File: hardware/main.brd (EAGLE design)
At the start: 96.5 x 65.5 mm, 79 parts, among them U1 TMS320F28069_PN_80, U10 TXB0101_DBV_6, U2 TXB0101_DBV_6, U3 SN74ABT541B_DW_20, U4 SN74LVC1G04_DBV_5, U5 SN74LVC4245A_DW_24, U7 Value, U8 Value, U9 SN74LVC4245A_DW_24

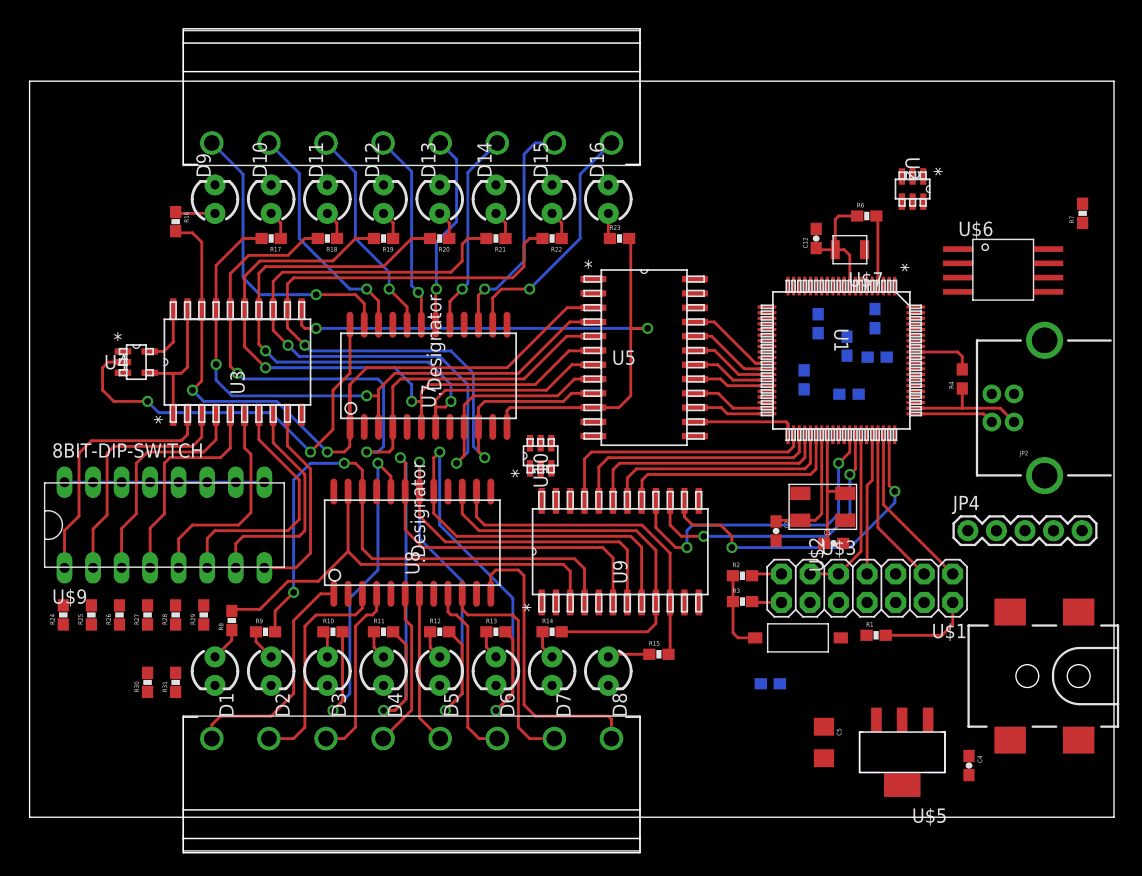
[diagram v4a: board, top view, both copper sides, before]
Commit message: Finished routing all signals traces. 3Vcc, 5Vcc, GND not yet routed. Signal traces need to be reviewed and cleaned up.
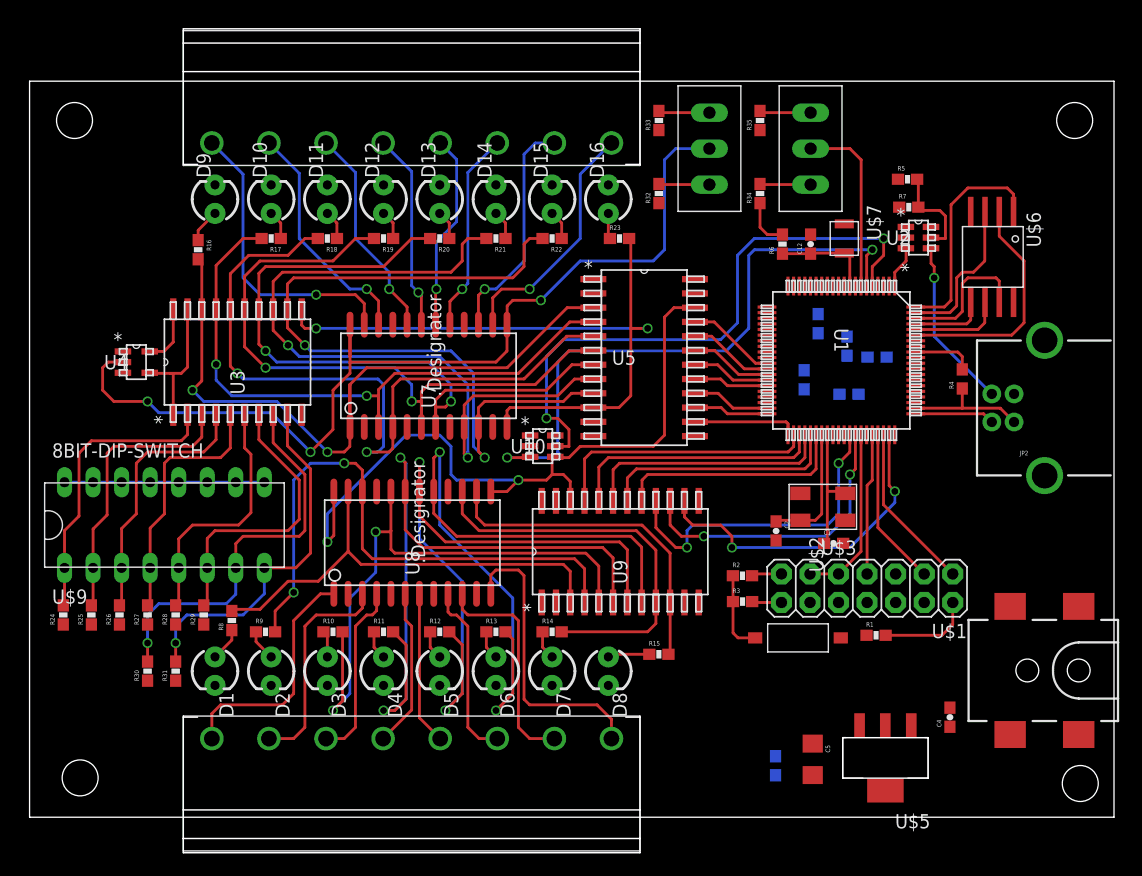
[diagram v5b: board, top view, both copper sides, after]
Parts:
- removed JP4: (no value), SparkFun-Connectors:1X05
- added R32, R33, R34, R35: 1K, SparkFun-Resistors:0603-RES
- added U$10, U$11: USER_SLIDE, ControllerCard:USER_SLIDE_SWITCH
- moved R7 15.5 mm to (78.2, 54.3), turned to 0 degrees
- moved R5 12.7 mm to (78.1, 56.8), flipped to the top, turned to 0 degrees
- moved R6 7.91 mm to (67.0, 51.0), turned to 90 degrees
- moved C6 7.31 mm to (66.4, 4.58), turned to 90 degrees
- moved C4 4.62 mm to (81.9, 8.90), turned to 90 degrees
- moved U2 4.35 mm to (79.1, 51.6), turned to 0 degrees
- moved R16 3.20 mm to (15.0, 50.5)
- moved C5 1.80 mm to (69.7, 5.15)
- moved U$5 1.58 mm to (76.2, 5.28)
- moved U$6 1.46 mm to (85.7, 49.9), turned to 270 degrees
- moved U$7 1.12 mm to (72.5, 51.5), turned to 270 degrees
- moved R30 1.00 mm to (10.5, 13.0)
- moved R31 1.00 mm to (13.0, 13.0)
- moved U10 0.88 mm to (45.7, 33.0), turned to 0 degrees
- moved C12 0.71 mm to (69.5, 51.0)
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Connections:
- new net N$29: R33.2, U$10.3
- new net N$38: R32.2, U$10.1
- new net N$39: R34.2, U$11.1
- new net N$40: R35.2, U$11.3
- net 3.3V: now also R34.1; no longer JP4.4
- net 5V: now also R32.1; no longer JP4.5
- net ENEXT: now also U1.5; no longer U1.7
- net GND: now also R33.1, R35.1; no longer JP4.1
- net INSEL: now also U$10.2; no longer JP4.3
- net RUNSEL: now also U$11.2, U1.7; no longer JP4.2, U1.5
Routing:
- net !BUFEN!: track 0.00 -> 65.9 mm, vias 0 -> 2
- net ENEXT: track 0.00 -> 61.7 mm, vias 0 -> 2
- net !ENEXT!: track 0.00 -> 55.2 mm, vias 0 -> 2
- net INSEL: track 37.6 -> 87.3 mm, vias 2 -> 3
- net SPISOMI: track 0.00 -> 20.9 mm
- net !FLASHEN!: track 0.00 -> 19.9 mm
- net LEDOUT3: track 34.0 -> 53.7 mm
- net RUNSEL: track 0.00 -> 16.2 mm
- net N$2: track 0.00 -> 15.2 mm, vias 0 -> 1
- net SW7: track 20.3 -> 35.4 mm, vias 0 -> 1
- net SW8: track 17.8 -> 32.4 mm, vias 0 -> 1
- net !FLASHWP!: track 0.00 -> 13.9 mm
- net !FLASHHOLD!: track 0.00 -> 12.4 mm
- net SPICLK: track 0.00 -> 8.26 mm
- net SPISIMO: track 0.00 -> 6.65 mm
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
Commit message: Finished re-routing clock and JTAG. Begun re-route of output stage.
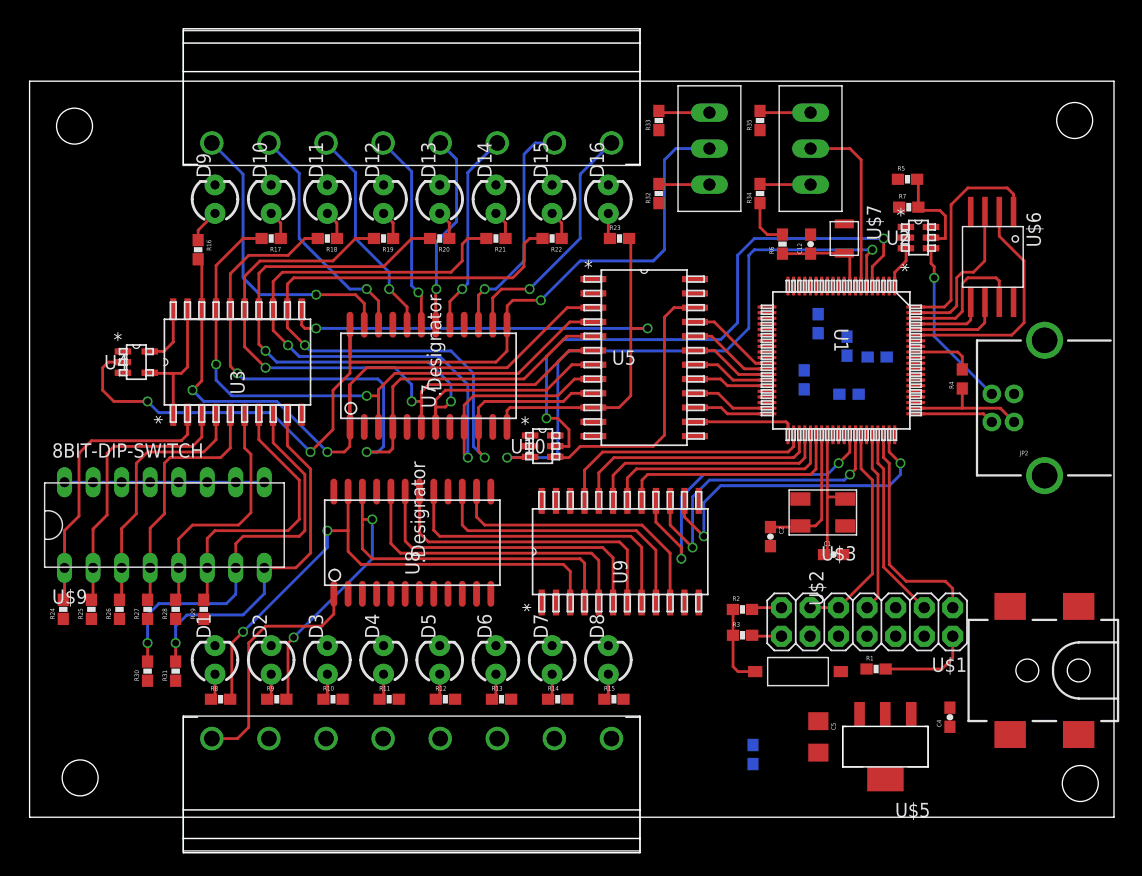
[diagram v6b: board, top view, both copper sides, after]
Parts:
- moved R8 7.07 mm to (17.0, 10.5), turned to 0 degrees
- moved R9 6.08 mm to (22.0, 10.5)
- moved R11 6.02 mm to (32.0, 10.5)
- moved R12 6.02 mm to (37.0, 10.5)
- moved R13 6.02 mm to (42.0, 10.5)
- moved R14 6.02 mm to (47.0, 10.5)
- moved R10 6.00 mm to (27.0, 10.5)
- moved R15 5.66 mm to (52.0, 10.5)
- moved R1 3.00 mm to (75.3, 13.2)
- moved R2 3.00 mm to (63.4, 18.5)
- moved R3 3.00 mm to (63.5, 16.2)
- moved U$1 3.00 mm to (82.2, 18.6)
- moved U$2 3.00 mm to (68.4, 13.0)
- moved C6 2.24 mm to (64.4, 5.58)
- moved C5 2.06 mm to (70.2, 7.15)
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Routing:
- net !BUFEN!: track 65.9 -> 24.3 mm, vias 2 -> 0
- net LEDOUT6: track 64.6 -> 27.5 mm, vias 2 -> 0
- net LEDOUT4: track 63.1 -> 27.5 mm, vias 2 -> 0
- net LEDOUT5: track 61.6 -> 27.5 mm, vias 2 -> 0
- net N$17: track 26.3 -> 0.00 mm
- net LEDOUT3: track 53.7 -> 27.5 mm, vias 2 -> 0
- net N$18: track 19.9 -> 0.00 mm
- net N$14: track 19.7 -> 0.00 mm
- net N$15: track 16.0 -> 0.00 mm
- net N$19: track 15.9 -> 0.00 mm
- net N$16: track 14.2 -> 0.00 mm
- net N$20: track 13.6 -> 0.00 mm
- net LEDOUT7: track 35.8 -> 25.8 mm
- net LEDOUT1: track 41.1 -> 49.0 mm, vias 0 -> 2
- net TMS: track 14.9 -> 20.0 mm
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
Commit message: Finished cleaning up routing. Updated user connectors to have 10 pins.
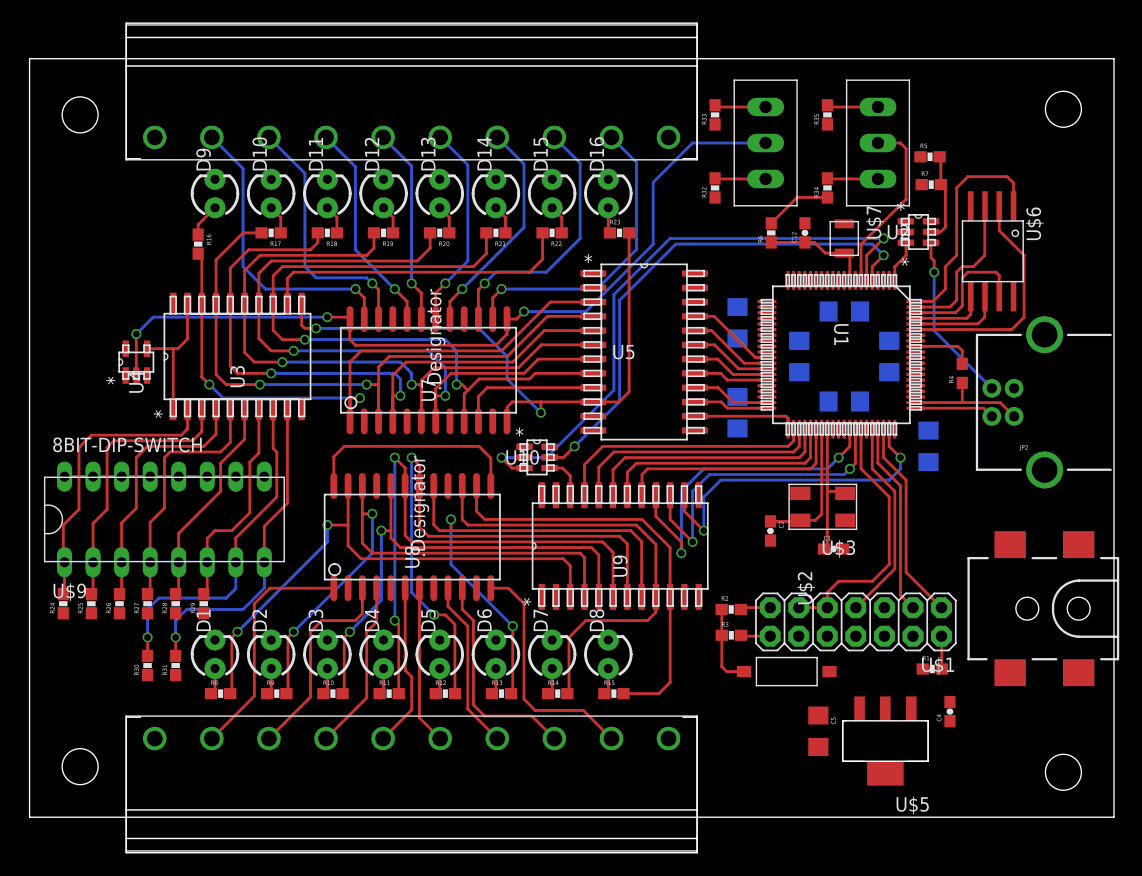
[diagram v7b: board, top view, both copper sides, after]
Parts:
- added C3: 2.2UF, SparkFun-Capacitors:1206
- C10, C11, C6, C7, C8, C9: value 2.2uF -> 2.2UF; device SparkFun-Capacitors:0603-CAP -> SparkFun-Capacitors:1206
- moved C6 31.6 mm to (80.0, 33.0), turned to 270 degrees
- moved C11 7.30 mm to (72.5, 37.0), turned to 0 degrees
- moved C7 6.61 mm to (63.0, 36.0)
- moved R34 6.02 mm to (71.0, 56.0)
- moved R35 6.02 mm to (71.0, 62.5)
- moved U$11 6.02 mm to (75.5, 60.0)
- moved JP1 5.50 mm to (93.4, 18.6)
- moved R32 5.02 mm to (61.0, 56.0)
- moved R33 5.02 mm to (61.0, 62.5)
- moved U$10 5.02 mm to (65.5, 60.0)
- moved R1 5.00 mm to (80.3, 13.2)
- moved C9 4.99 mm to (72.5, 45.0), turned to 180 degrees
- moved C10 4.91 mm to (76.5, 41.0), turned to 90 degrees
- moved C8 4.34 mm to (68.5, 41.0)
- moved R5 2.83 mm to (80.1, 58.8)
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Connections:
- net 3.3V: now also C10.1, C11.1, C3.1, C6.1, C7.1, C8.1, C9.1; no longer C10.2, C11.2, C6.2, C7.2, C8.2, C9.2
- net 5V: now also U$4.1, U$8.10
- net GND: now also C10.2, C11.2, C3.2, C6.2, C7.2, C8.2, C9.2, U$4.10, U$8.1; no longer C10.1, C11.1, C6.1, C7.1, C8.1, C9.1
- net N$13: now also U$4.2; no longer U$4.P$1
- net N$14: now also U$4.3; no longer U$4.P$2
- net N$15: now also U$4.4; no longer U$4.P$3
- net N$16: now also U$4.5; no longer U$4.P$4
- net N$17: now also U$4.9; no longer U$4.P$8
- net N$18: now also U$4.8; no longer U$4.P$7
- net N$19: now also U$4.7; no longer U$4.P$6
- net N$20: now also U$4.6; no longer U$4.P$5
- net N$21: now also U$8.9; no longer U$8.P$8
- net N$22: now also U$8.8; no longer U$8.P$7
- net N$23: now also U$8.7; no longer U$8.P$6
- net N$24: now also U$8.6; no longer U$8.P$5
- net N$25: now also U$8.2; no longer U$8.P$1
- net N$26: now also U$8.3; no longer U$8.P$2
- net N$27: now also U$8.4; no longer U$8.P$3
- net N$28: now also U$8.5; no longer U$8.P$4
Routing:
- net LEDIN7: track 71.0 -> 40.8 mm, vias 2 -> 0
- net LEDOUT5: track 27.5 -> 53.5 mm, vias 0 -> 2
- net LEDOUT4: track 27.5 -> 51.5 mm, vias 0 -> 2
- net N$17: track 0.00 -> 21.3 mm
- net N$18: track 0.00 -> 19.2 mm
- net LEDOUT6: track 27.5 -> 46.3 mm, vias 0 -> 2
- net N$14: track 0.00 -> 18.6 mm
- net LEDOUT3: track 27.5 -> 44.3 mm, vias 0 -> 2
- net N$15: track 0.00 -> 15.2 mm
- net N$19: track 0.00 -> 15.2 mm
- net LEDOUT7: track 25.8 -> 40.9 mm
- net N$16: track 0.00 -> 14.7 mm
- net N$20: track 0.00 -> 14.1 mm
- net INSEL: track 87.3 -> 73.9 mm
- net LEDOUT8: track 25.2 -> 37.4 mm
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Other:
- board size 96.5 x 65.5 mm -> 96.5 x 67.5 mm

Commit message: Checked and edited component layouts. Updated and checked passive component values. Double checked chip peripherals.
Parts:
- added C13, C14, C15, C16: 0.1uF, SparkFun-Capacitors:1206
- C4: value 0.22uF -> 0.47uF
- R5, R7: value 100/.25W -> 10K
- moved R1 5.17 mm to (75.2, 12.8), turned to 180 degrees
- moved C1 0.50 mm to (71.5, 23.4)
- moved C2 0.50 mm to (65.4, 25.5)
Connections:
- net 3.3V: now also C13.1, C15.1
- net 5V: now also C14.1, C16.1
- net GND: now also C13.2, C14.2, C15.2, C16.2; no longer U$2.P$1
- net N$1: now also U$2.P$1
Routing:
- net 3.3V: track 18.7 -> 28.4 mm
- net X1: track 12.5 -> 13.1 mm
- net X2: track 12.4 -> 12.9 mm
